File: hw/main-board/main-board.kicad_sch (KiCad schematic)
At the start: 66 parts, among them J1 USB_C_Receptacle_USB2.0_16P, J2 S4B-XH-A_LF__SN_, J3 S4B-XH-A_LF__SN_, J4 Conn_ARM_JTAG_SWD_10, Q1 AONR21307, U1 HUSB238_xxxDD, U2 AP63205WU, U3 AP2112K-3.3, U4 PTR54L, U5 TMC2226-SA, U6 TMC2226-SA, U7 KTD2026BEWE-TR

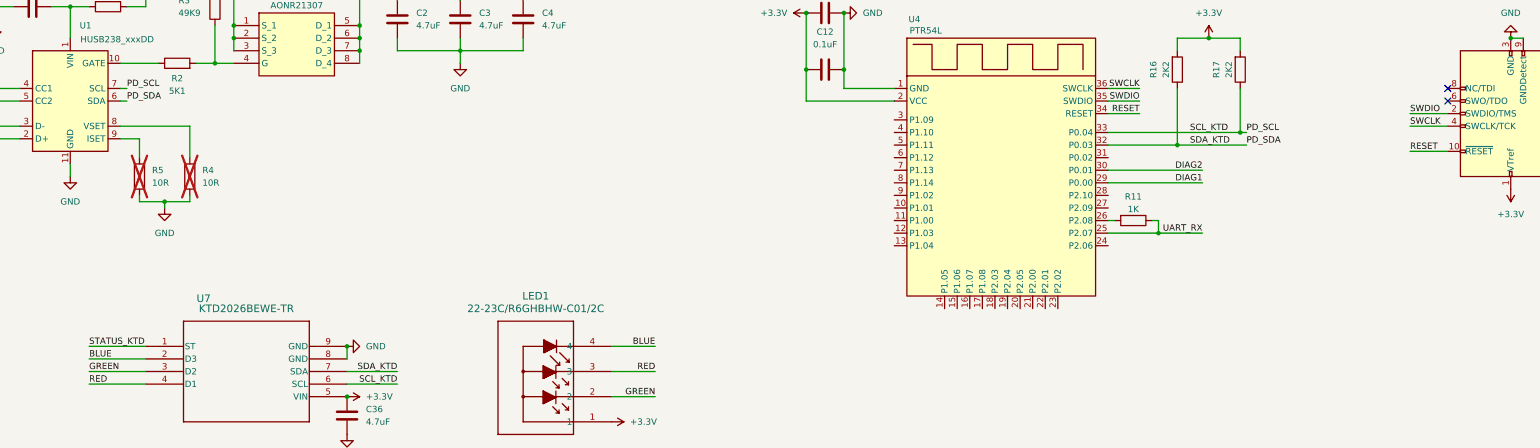
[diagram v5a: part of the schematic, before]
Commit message: Fix connection TMC2226 to NRF
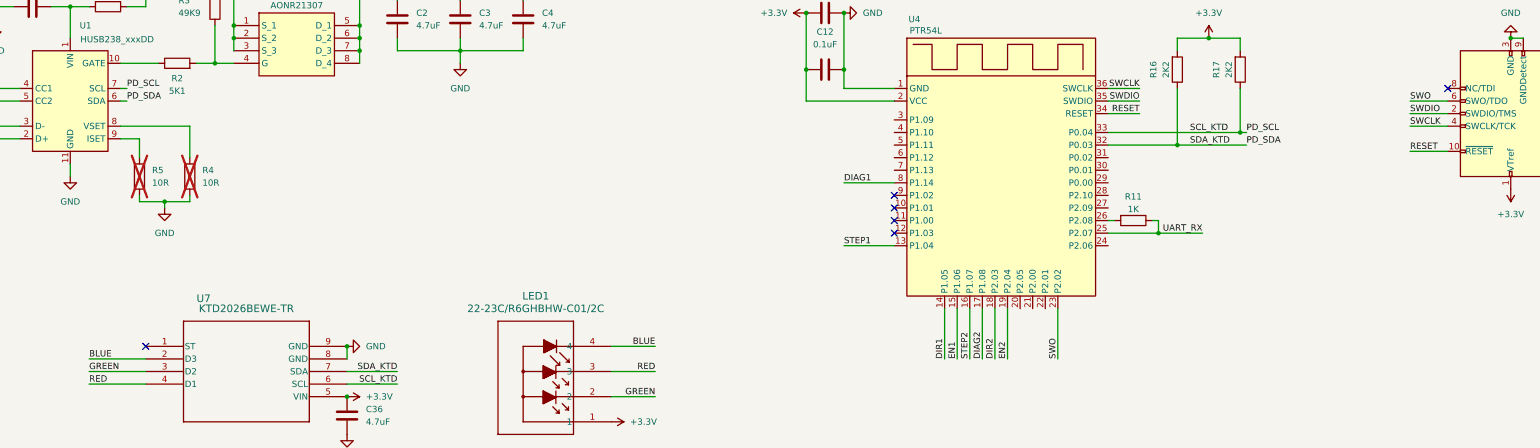
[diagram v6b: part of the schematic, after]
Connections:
- net DIAG1: now also U4.8 (P1.14); no longer U4.29 (P0.00)
- net DIAG2: now also U4.17 (P1.08); no longer U4.30 (P0.01)
- net DIR1: now also U4.14 (P1.05)
- net DIR2: now also U4.18 (P2.03)
- net EN1: now also U4.15 (P1.06)
- net EN2: now also U4.19 (P2.04)
- net STEP1: now also U4.13 (P1.04)
- net STEP2: now also U4.16 (P1.07)
- net SWO: now reaches U4.23 (P2.02)
- net SWO: now also J4.6 (SWO/TDO)
- net STATUS_KTD: no longer names the net of U7.1 (ST)
- no-connect marks 12 -> 16
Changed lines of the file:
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@@
+	)
+	(no_connect
+		(at 92.71 109.22)
+	)
+	(no_connect
+		(at 243.84 78.74)
 	)
 	(no_connect
@@
 	)
 	(no_connect
+		(at 243.84 83.82)
+	)
+	(no_connect
 		(at 55.88 80.01)
 	)
@@
 	)
 	(no_connect
+		(at 243.84 86.36)
+	)
+	(no_connect
 		(at 215.9 231.14)
 	)
@@
 	)
 	(no_connect
-		(at 355.6 59.69)
+		(at 243.84 81.28)
 	)
 	(wire
@@
 	(wire
 		(pts
+			(xy 259.08 101.6) (xy 259.08 111.76)
+		)
+		(stroke
+			(width 0)
+			(type default)
+		)
+	)
+	(wire
+		(pts
+			(xy 233.68 88.9) (xy 243.84 88.9)
+		)
+		(stroke
+			(width 0)
+			(type default)
+		)
+	)
+	(wire
+		(pts
 			(xy 88.9 152.4) (xy 104.14 152.4)
 		)
@@
 	(wire
 		(pts
+			(xy 276.86 101.6) (xy 276.86 111.76)
+		)
+		(stroke
+			(width 0)
+			(type default)
+		)
+	)
+	(wire
+		(pts
 			(xy 347.98 214.63) (xy 349.25 214.63)
 		)
@@
 	(wire
 		(pts
+			(xy 256.54 101.6) (xy 256.54 111.76)
+		)
+		(stroke
+			(width 0)
+			(type default)
+		)
+	)
+	(wire
+		(pts
 			(xy 96.52 232.41) (xy 110.49 232.41)
 		)
@@
 	(wire
 		(pts
+			(xy 254 101.6) (xy 254 111.76)
+		)
+		(stroke
+			(width 0)
+			(type default)
+		)
+	)
+	(wire
+		(pts
 			(xy 194.31 167.64) (xy 171.45 167.64)
 		)
@@
 	(wire
 		(pts
+			(xy 233.68 76.2) (xy 243.84 76.2)
+		)
+		(stroke
+			(width 0)
+			(type default)
+		)
+	)
+	(wire
+		(pts
 			(xy 81.28 116.84) (xy 92.71 116.84)
 		)
@@
 	(wire
 		(pts
-			(xy 81.28 109.22) (xy 92.71 109.22)
-		)
-		(stroke
-			(width 0)
-			(type default)
-		)
-	)
-	(wire
-		(pts
 			(xy 307.34 175.26) (xy 307.34 177.8)
 		)
@@
 	(wire
 		(pts
-			(xy 287.02 76.2) (xy 306.07 76.2)
-		)
-		(stroke
-			(width 0)
-			(type default)
-		)
-	)
-	(wire
-		(pts
 			(xy 326.39 157.48) (xy 326.39 165.1)
 		)
@@
 	(wire
 		(pts
+			(xy 261.62 101.6) (xy 261.62 111.76)
+		)
+		(stroke
+			(width 0)
+			(type default)
+		)
+	)
+	(wire
+		(pts
 			(xy 77.47 232.41) (xy 77.47 234.95)
 		)
@@
 	(wire
 		(pts
+			(xy 266.7 101.6) (xy 266.7 111.76)
+		)
+		(stroke
+			(width 0)
+			(type default)
+		)
+	)
+	(wire
+		(pts
 			(xy 307.34 182.88) (xy 316.23 182.88)
 		)
@@
 	(wire
 		(pts
+			(xy 264.16 101.6) (xy 264.16 111.76)
+		)
+		(stroke
+			(width 0)
+			(type default)
+		)
+	)
+	(wire
+		(pts
 			(xy 287.02 59.69) (xy 293.37 59.69)
 		)
@@
 	(wire
 		(pts
+			(xy 347.98 59.69) (xy 355.6 59.69)
+		)
+		(stroke
+			(width 0)
+			(type default)
+		)
+	)
+	(wire
+		(pts
 			(xy 110.49 240.03) (xy 110.49 242.57)
 		)
@@
 		(pts
 			(xy 346.71 213.36) (xy 347.98 213.36)
-		)
-		(stroke
-			(width 0)
-			(type default)
-		)
-	)
-	(wire
-		(pts
-			(xy 287.02 73.66) (xy 306.07 73.66)
 		)
 		(stroke
@@
 		)
 	)
+	(label "SWO"
+		(at 347.98 59.69 0)
+		(effects
+			(font
+				(size 1.27 1.27)
+			)
+			(justify left bottom)
+		)
+	)
 	(label "SWDIO"
 		(at 293.37 59.69 180)
@@
 		)
 	)
+	(label "STEP2"
+		(at 259.08 111.76 90)
+		(effects
+			(font
+				(size 1.27 1.27)
+			)
+			(justify left bottom)
+		)
+	)
+	(label "DIR1"
+		(at 254 111.76 90)
+		(effects
+			(font
+				(size 1.27 1.27)
+			)
+			(justify left bottom)
+		)
+	)
 	(label "UART_RX"
 		(at 189.23 182.88 0)
@@
 		)
 	)
+	(label "EN1"
+		(at 256.54 111.76 90)
+		(effects
+			(font
+				(size 1.27 1.27)
+			)
+			(justify left bottom)
+		)
+	)
 	(label "GREEN"
 		(at 81.28 114.3 0)
@@
 		)
 	)
+	(label "STEP1"
+		(at 233.68 88.9 0)
+		(effects
+			(font
+				(size 1.27 1.27)
+			)
+			(justify left bottom)
+		)
+	)
 	(label "SWDIO"
 		(at 347.98 62.23 0)
@@
 		)
 	)
+	(label "EN2"
+		(at 266.7 111.76 90)
+		(effects
+			(font
+				(size 1.27 1.27)
+			)
+			(justify left bottom)
+		)
+	)
 	(label "DIR2"
 		(at 307.34 190.5 0)
@@
 		)
 	)
+	(label "DIR2"
+		(at 264.16 111.76 90)
+		(effects
+			(font
+				(size 1.27 1.27)
+			)
+			(justify left bottom)
+		)
+	)
 	(label "GREEN"
 		(at 195.58 119.38 180)
@@
 		)
 	)
-	(label "STATUS_KTD"
-		(at 81.28 109.22 0)
-		(effects
-			(font
-				(size 1.27 1.27)
-			)
-			(justify left bottom)
-		)
-	)
 	(label "PD_SDA"
 		(at 314.96 68.58 0)
@@
 	)
 	(label "DIAG1"
-		(at 306.07 76.2 180)
-		(effects
-			(font
-				(size 1.27 1.27)
-			)
-			(justify right bottom)
+		(at 233.68 76.2 0)
+		(effects
+			(font
+				(size 1.27 1.27)
+			)
+			(justify left bottom)
 		)
 	)
@@
 		)
 	)
+	(label "SWO"
+		(at 276.86 111.76 90)
+		(effects
+			(font
+				(size 1.27 1.27)
+			)
+			(justify left bottom)
+		)
+	)
 	(label "EN2"
 		(at 307.34 203.2 0)
@@
 	)
 	(label "DIAG2"
-		(at 306.07 73.66 180)
-		(effects
-			(font
-				(size 1.27 1.27)
-			)
-			(justify right bottom)
-		)
-	)
+		(at 261.62 111.76 90)
+		(effects
+			(font
+				(size 1.27 1.27)
+			)
+			(justify left bottom)
+		)
+	)

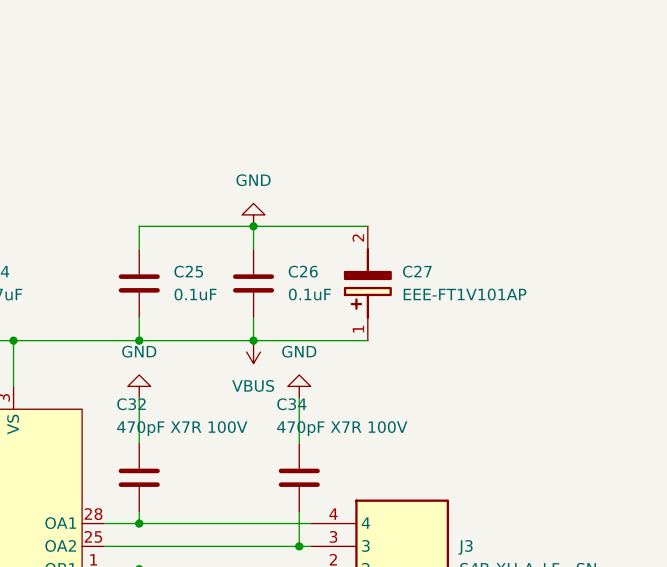
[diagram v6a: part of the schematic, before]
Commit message: Remove excessive cap for driver
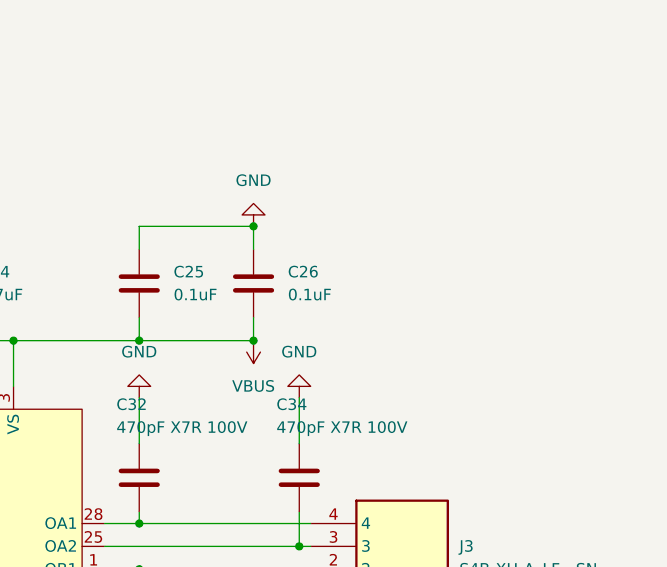
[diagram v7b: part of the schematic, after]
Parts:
- removed C27: EEE-FT1V101AP, EEE1AA101SP, symbol Samacsys:EEE-FT1V101AP
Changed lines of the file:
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@@
 	(wire
 		(pts
-			(xy 363.22 147.32) (xy 375.92 147.32)
-		)
-		(stroke
-			(width 0)
-			(type default)
-		)
-	)
-	(wire
-		(pts
 			(xy 106.68 36.83) (xy 110.49 36.83)
 		)
@@
 	(wire
 		(pts
-			(xy 363.22 160.02) (xy 375.92 160.02)
-		)
-		(stroke
-			(width 0)
-			(type default)
-		)
-	)
-	(wire
-		(pts
 			(xy 307.34 210.82) (xy 316.23 210.82)
 		)
@@
 					(unit 1)
 				)
-			)
-		)
-	)
-	(symbol
-		(lib_id "Samacsys:EEE-FT1V101AP")
-		(at 375.92 160.02 90)
-		(unit 1)
-		(body_style 1)
-		(exclude_from_sim no)
-		(in_bom yes)
-		(on_board yes)
-		(in_pos_files yes)
-		(dnp no)
-		(fields_autoplaced yes)
-		(property "Reference" "C27"
-			(at 379.73 152.3999 90)
-			(show_name no)
-			(do_not_autoplace no)
-			(effects
-				(font
-					(size 1.27 1.27)
-				)
-				(justify right)
-			)
-		)
-		(property "Value" "EEE-FT1V101AP"
-			(at 379.73 154.9399 90)
-			(show_name no)
-			(do_not_autoplace no)
-			(effects
-				(font
-					(size 1.27 1.27)
-				)
-				(justify right)
-			)
-		)
-		(property "Footprint" "EEE1AA101SP"
-			(at 472.11 151.13 0)
-			(hide yes)
-			(show_name no)
-			(do_not_autoplace no)
-			(effects
-				(font
-					(size 1.27 1.27)
-				)
-				(justify left top)
-			)
-		)
-		(property "Datasheet" "http://industrial.panasonic.com/cdbs/www-data/pdf/RDE0000/ABA0000C1240.pdf"
-			(at 572.11 151.13 0)
-			(hide yes)
-			(show_name no)
-			(do_not_autoplace no)
-			(effects
-				(font
-					(size 1.27 1.27)
-				)
-				(justify left top)
-			)
-		)
-		(property "Description" "Aluminum Electrolytic Capacitors - SMD 100uF 35volts 6.3x5.8mm SMD"
-			(at 375.92 160.02 0)
-			(hide yes)
-			(show_name no)
-			(do_not_autoplace no)
-			(effects
-				(font
-					(size 1.27 1.27)
-				)
-			)
-		)
-		(property "Height" "7.8"
-			(at 772.11 151.13 0)
-			(hide yes)
-			(show_name no)
-			(do_not_autoplace no)
-			(effects
-				(font
-					(size 1.27 1.27)
-				)
-				(justify left top)
-			)
-		)
-		(property "Manufacturer_Name" "Panasonic"
-			(at 872.11 151.13 0)
-			(hide yes)
-			(show_name no)
-			(do_not_autoplace no)
-			(effects
-				(font
-					(size 1.27 1.27)
-				)
-				(justify left top)
-			)
-		)
-		(property "Manufacturer_Part_Number" "EEE-FT1V101AP"
-			(at 972.11 151.13 0)
-			(hide yes)
-			(show_name no)
-			(do_not_autoplace no)
-			(effects
-				(font
-					(size 1.27 1.27)
-				)
-				(justify left top)
-			)
-		)
-		(property "Mouser Part Number" "667-EEE-FT1V101AP"
-			(at 1072.11 151.13 0)
-			(hide yes)
-			(show_name no)
-			(do_not_autoplace no)
-			(effects
-				(font
-					(size 1.27 1.27)
-				)
-				(justify left top)
-			)
-		)
-		(property "Mouser Price/Stock" "https://www.mouser.co.uk/ProductDetail/Panasonic/EEE-FT1V101AP?qs=CMJjuEs1%252BuEsbOqam%2FkTqg%3D%3D"
-			(at 1172.11 151.13 0)
-			(hide yes)
-			(show_name no)
-			(do_not_autoplace no)
-			(effects
-				(font
-					(size 1.27 1.27)
-				)
-				(justify left top)
-			)
-		)
-		(property "Arrow Part Number" "EEE-FT1V101AP"
-			(at 1272.11 151.13 0)
-			(hide yes)
-			(show_name no)
-			(do_not_autoplace no)
-			(effects
-				(font
-					(size 1.27 1.27)
-				)
-				(justify left top)
-			)
-		)
-		(property "Arrow Price/Stock" "https://www.arrow.com/en/products/eeeft1v101ap/panasonic.html?utm_currency=USD&region=nac"
-			(at 1372.11 151.13 0)
-			(hide yes)
-			(show_name no)
-			(do_not_autoplace no)
-			(effects
-				(font
-					(size 1.27 1.27)
-				)
-				(justify left top)
-			)
-		)
-		(pin "2"
-		)
-		(pin "1"
-		)
-		(instances
-			(project "main-board"
-				(path "/fe215afa-a228-4dbb-8560-a0753323a3f2"
-					(reference "C27")
-					(unit 1)
-				)

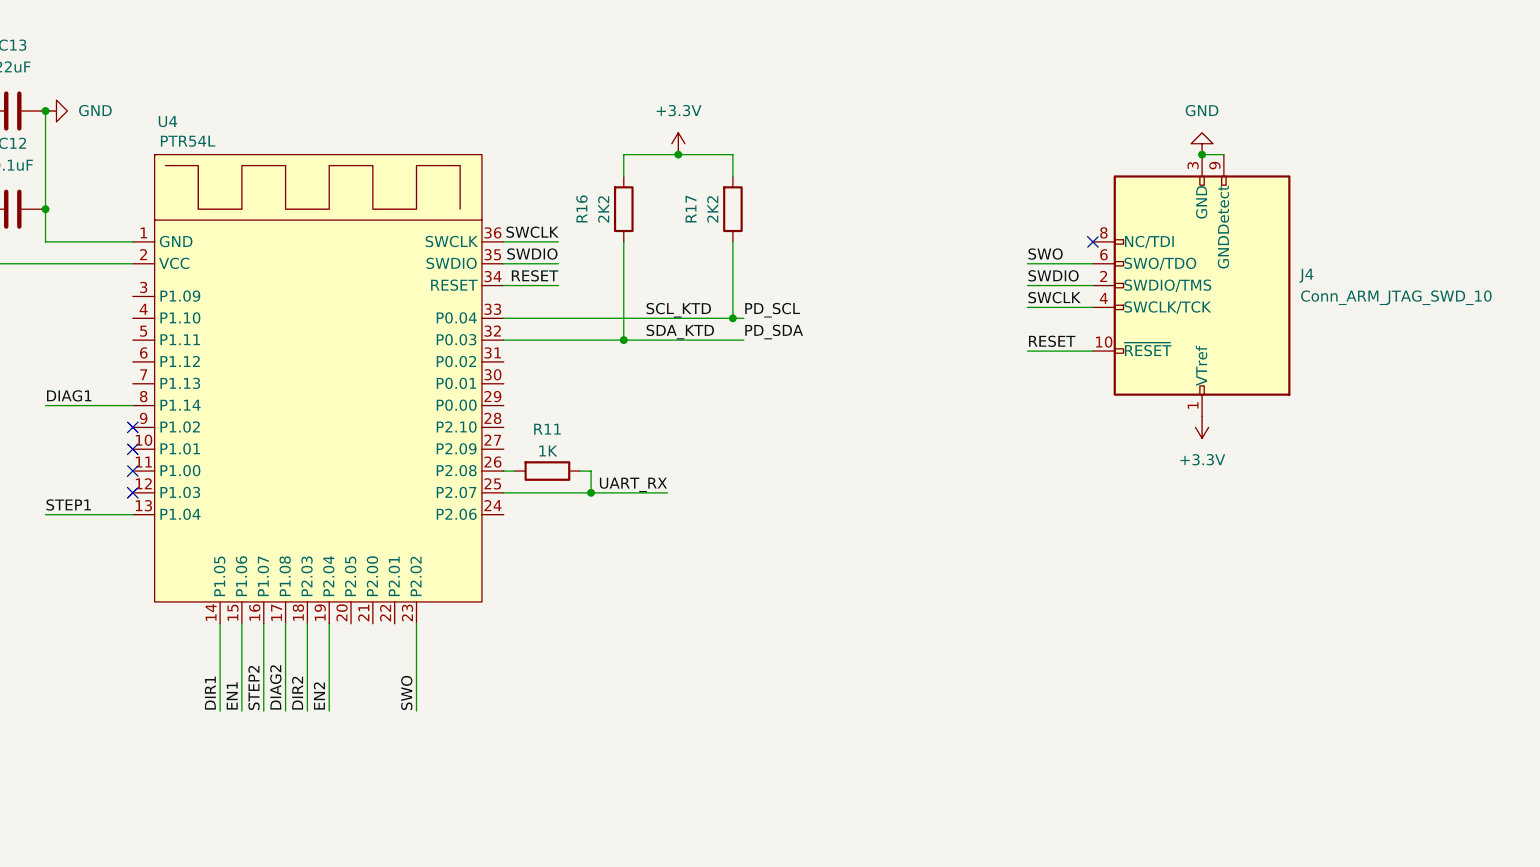
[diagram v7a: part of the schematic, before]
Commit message: Add button
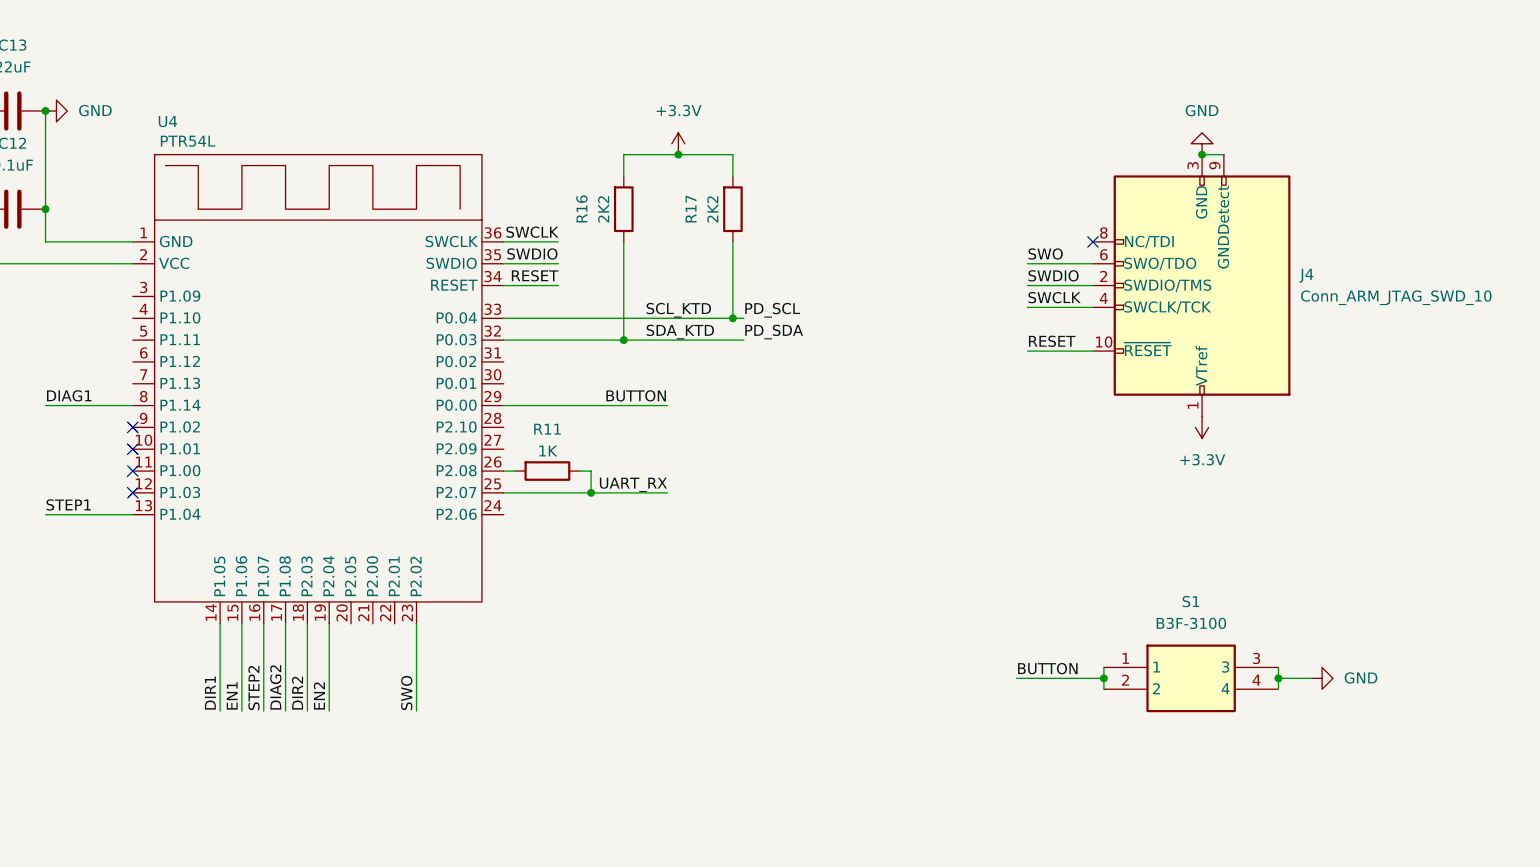
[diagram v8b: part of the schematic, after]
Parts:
- added S1: B3F-3100, B3F3100, symbol Samacsys:B3F-3100
- J2: footprint Samacsys:S4BXHALFSN -> S4BXHALFSN
- L1: footprint Samacsys:INDPM4441X200N -> INDPM4441X200N
- Q1: footprint Samacsys:DFN_3X3_EP -> DFN_3X3_EP
- U7: footprint Project_Specific_Parts:UTDFN8_1P5X1P5_KIN -> UTDFN8_1P5X1P5_KIN
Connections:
- net GND: now also S1.3, S1.4
- net BUTTON: now reaches U4.29 (P0.00)
- net BUTTON: now also S1.1, S1.2
